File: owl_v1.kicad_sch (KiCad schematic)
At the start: 24 parts, among them J1 USB_C_Receptacle_USB2.0_14P, SW1 SW_SPDT, U1 STM32F103C8T6, U2 XC6206P302, Y1 8MHz, Y2 32k768

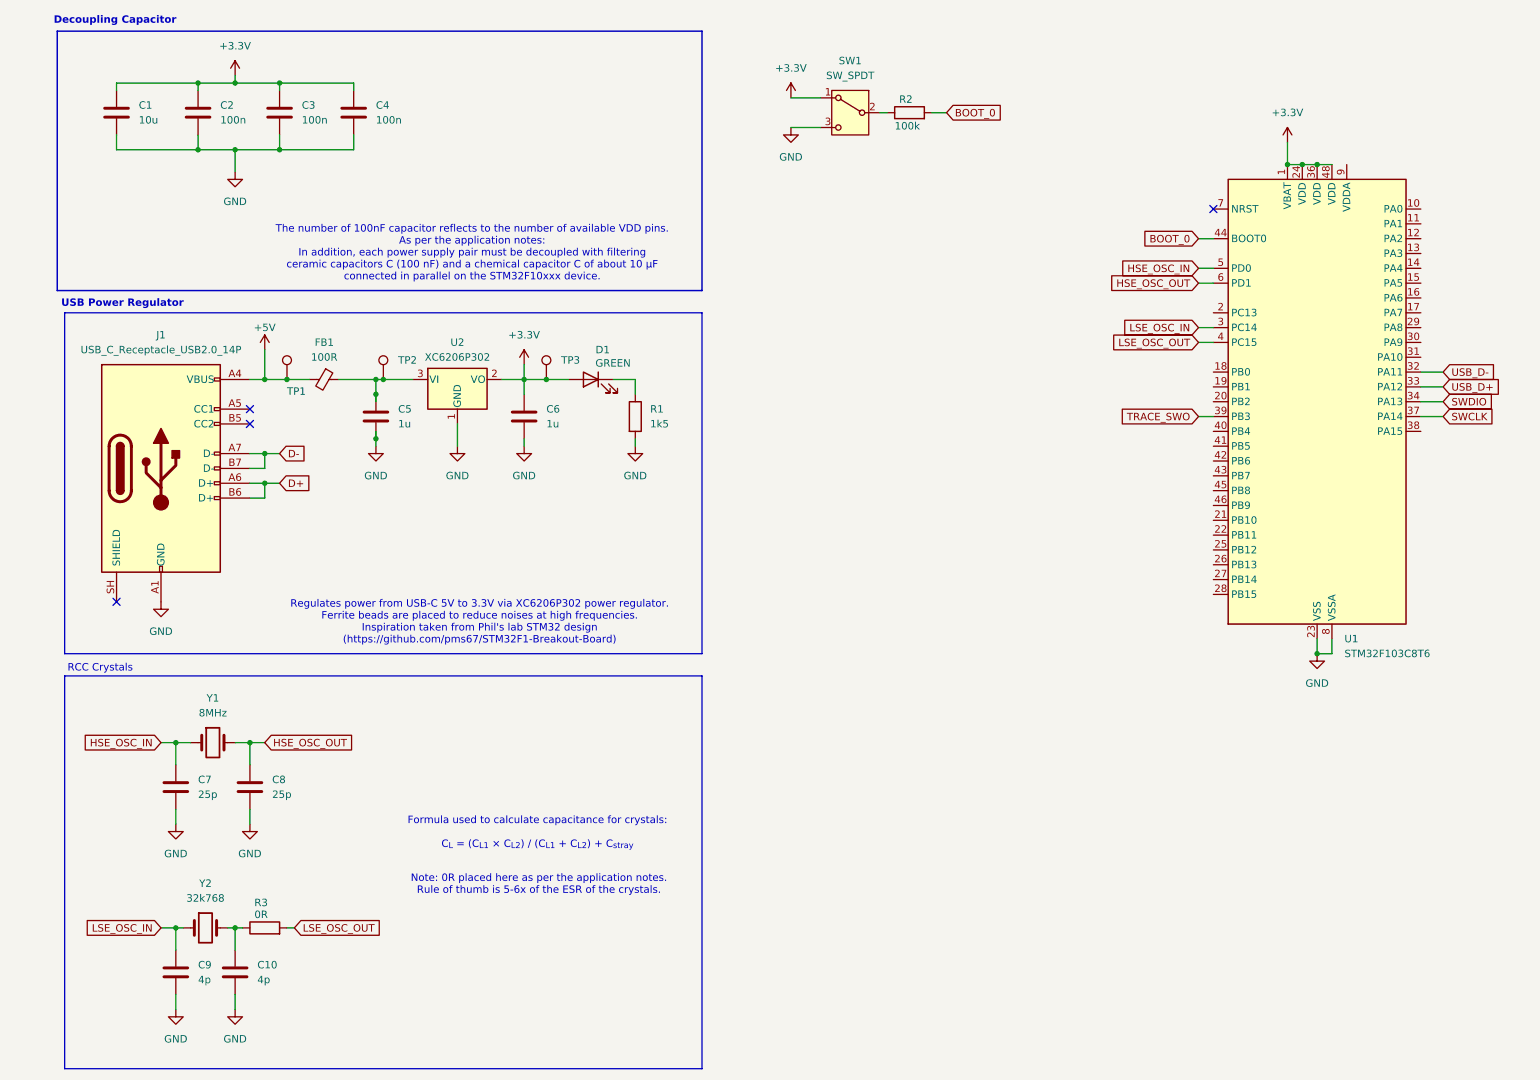
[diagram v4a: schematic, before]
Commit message: [feat] Initial implementation of usb-uart bridge with FT230
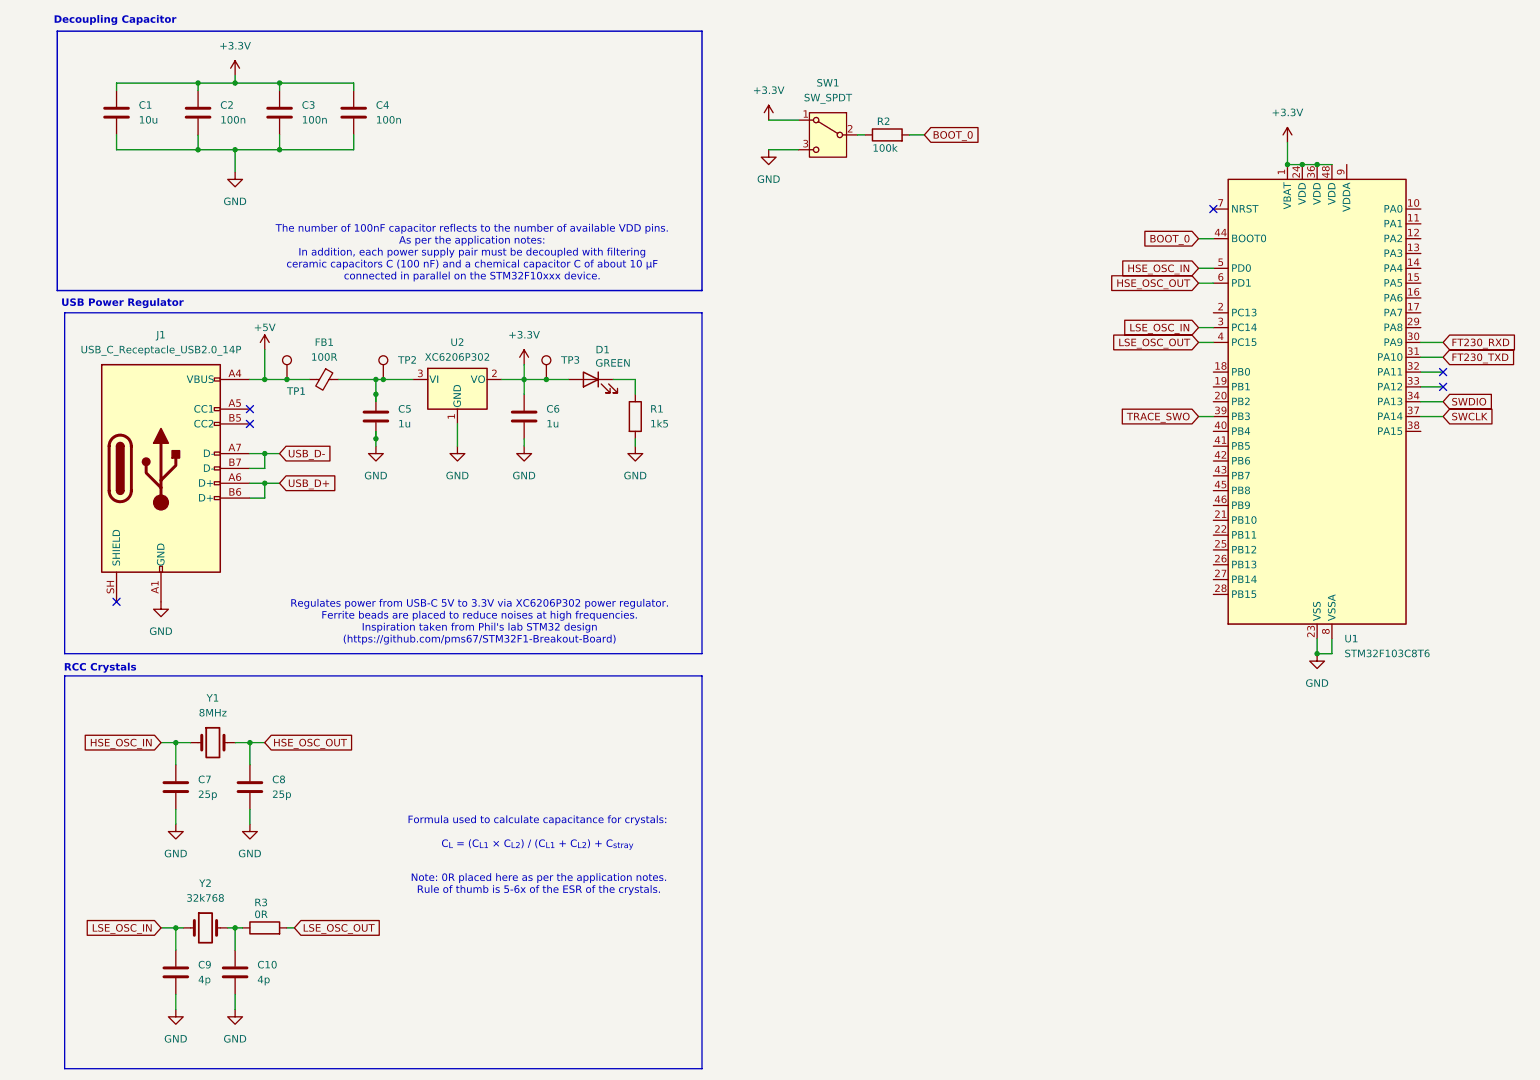
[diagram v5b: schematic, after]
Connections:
- net D+ is gone; now on net USB_D+: J1.A6 (D+), J1.B6 (D+)
- net D- is gone; now on net USB_D-: J1.A7 (D-), J1.B7 (D-)
- net USB_D+: no longer U1.33 (PA12)
- net USB_D-: no longer U1.32 (PA11)
- net FT230_RXD: now reaches U1.30 (PA9)
- net FT230_TXD: now reaches U1.31 (PA10)
- no-connect marks 4 -> 6
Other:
- moved on the sheet: R2, SW1
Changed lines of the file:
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@@
 			(font
 				(size 1.27 1.27)
+				(thickness 0.254)
+				(bold yes)
 			)
 		)
@@
 	)
 	(no_connect
+		(at 260.35 76.2)
+	)
+	(no_connect
 		(at 33.02 115.57)
 	)
@@
 	)
 	(no_connect
+		(at 260.35 78.74)
+	)
+	(no_connect
 		(at 220.98 48.26)
 	)
@@
 	(wire
 		(pts
+			(xy 256.54 73.66) (xy 260.35 73.66)
+		)
+		(stroke
+			(width 0)
+			(type default)
+		)
+	)
+	(wire
+		(pts
 			(xy 77.47 77.47) (xy 78.74 77.47)
 		)
@@
 	(wire
 		(pts
-			(xy 172.72 31.75) (xy 175.26 31.75)
+			(xy 168.91 35.56) (xy 171.45 35.56)
 		)
 		(stroke
@@
 	(wire
 		(pts
-			(xy 148.59 34.29) (xy 153.67 34.29)
+			(xy 144.78 38.1) (xy 149.86 38.1)
 		)
 		(stroke
@@
 	(wire
 		(pts
-			(xy 148.59 29.21) (xy 153.67 29.21)
+			(xy 144.78 33.02) (xy 149.86 33.02)
 		)
 		(stroke
@@
 	(wire
 		(pts
+			(xy 256.54 71.12) (xy 260.35 71.12)
+		)
+		(stroke
+			(width 0)
+			(type default)
+		)
+	)
+	(wire
+		(pts
 			(xy 233.68 36.83) (xy 233.68 40.64)
 		)
@@
 	(wire
 		(pts
-			(xy 163.83 31.75) (xy 165.1 31.75)
+			(xy 160.02 35.56) (xy 161.29 35.56)
 		)
 		(stroke
@@
 		)
 	)
+	(global_label "FT230_TXD"
+		(shape input)
+		(at 260.35 73.66 0)
+		(fields_autoplaced yes)
+		(effects
+			(font
+				(size 1.27 1.27)
+			)
+			(justify left)
+		)
+		(property "Intersheetrefs" "${INTERSHEET_REFS}"
+			(at 273.4346 73.66 0)
+			(hide yes)
+			(show_name no)
+			(do_not_autoplace no)
+			(effects
+				(font
+					(size 1.27 1.27)
+				)
+				(justify left)
+			)
+		)
+	)
 	(global_label "HSE_OSC_OUT"
 		(shape input)
@@
 		)
 	)
-	(global_label "USB_D+"
+	(global_label "FT230_RXD"
 		(shape input)
-		(at 260.35 78.74 0)
+		(at 260.35 71.12 0)
 		(fields_autoplaced yes)
 		(effects
@@
 		)
 		(property "Intersheetrefs" "${INTERSHEET_REFS}"
-			(at 270.9552 78.74 0)
+			(at 273.737 71.12 0)
 			(hide yes)
 			(show_name no)
@@
 		)
 	)
-	(global_label "D+"
+	(global_label "USB_D+"
 		(shape input)
 		(at 60.96 95.25 0)
@@
 		)
 		(property "Intersheetrefs" "${INTERSHEET_REFS}"
-			(at 66.7876 95.25 0)
+			(at 71.5652 95.25 0)
 			(hide yes)
 			(show_name no)
@@
 	(global_label "BOOT_0"
 		(shape input)
-		(at 175.26 31.75 0)
+		(at 171.45 35.56 0)
 		(fields_autoplaced yes)
 		(effects
@@
 		)
 		(property "Intersheetrefs" "${INTERSHEET_REFS}"
-			(at 185.3209 31.75 0)
+			(at 181.5109 35.56 0)
 			(hide yes)
 			(show_name no)
@@
 		)
 	)
-	(global_label "D-"
-		(shape input)
-		(at 60.96 90.17 0)
-		(fields_autoplaced yes)
-		(effects
-			(font
-				(size 1.27 1.27)
-			)
-			(justify left)
-		)
-		(property "Intersheetrefs" "${INTERSHEET_REFS}"
-			(at 66.7876 90.17 0)
-			(hide yes)
-			(show_name no)
-			(do_not_autoplace no)
-			(effects
-				(font
-					(size 1.27 1.27)
-				)
-				(justify left)
-			)
-		)
-	)
 	(global_label "USB_D-"
 		(shape input)
-		(at 260.35 76.2 0)
+		(at 60.96 90.17 0)
 		(fields_autoplaced yes)
 		(effects
@@
 		)
 		(property "Intersheetrefs" "${INTERSHEET_REFS}"
-			(at 270.9552 76.2 0)
+			(at 71.5652 90.17 0)
 			(hide yes)
 			(show_name no)
@@
 	(symbol
 		(lib_id "power:+3.3V")
-		(at 148.59 29.21 0)
+		(at 144.78 33.02 0)
 		(unit 1)
 		(body_style 1)
@@
 		(fields_autoplaced yes)
 		(property "Reference" "#PWR012"
-			(at 148.59 33.02 0)
+			(at 144.78 36.83 0)
 			(hide yes)
 			(show_name no)
@@
 		)
 		(property "Value" "+3.3V"
-			(at 148.59 24.13 0)
+			(at 144.78 27.94 0)
 			(show_name no)
 			(do_not_autoplace no)
@@
 		)
 		(property "Footprint" ""
-			(at 148.59 29.21 0)
+			(at 144.78 33.02 0)
 			(hide yes)
 			(show_name no)
@@
 		)
 		(property "Datasheet" ""
-			(at 148.59 29.21 0)
+			(at 144.78 33.02 0)
 			(hide yes)
 			(show_name no)
@@
 		)
 		(property "Description" "Power symbol creates a global label with name \"+3.3V\""
-			(at 148.59 29.21 0)
+			(at 144.78 33.02 0)
 			(hide yes)
 			(show_name no)
@@
 	(symbol
 		(lib_id "power:GND")
-		(at 148.59 34.29 0)
+		(at 144.78 38.1 0)
 		(unit 1)
 		(body_style 1)
@@
 		(fields_autoplaced yes)
 		(property "Reference" "#PWR013"
-			(at 148.59 40.64 0)
+			(at 144.78 44.45 0)
 			(hide yes)
 			(show_name no)
@@
 		)
 		(property "Value" "GND"
-			(at 148.59 39.37 0)
+			(at 144.78 43.18 0)
 			(show_name no)
 			(do_not_autoplace no)
@@
 		)
 		(property "Footprint" ""
-			(at 148.59 34.29 0)
+			(at 144.78 38.1 0)
 			(hide yes)
 			(show_name no)
@@
 		)
 		(property "Datasheet" ""
-			(at 148.59 34.29 0)
+			(at 144.78 38.1 0)
 			(hide yes)
 			(show_name no)
@@
 		)
 		(property "Description" "Power symbol creates a global label with name \"GND\" , ground"
-			(at 148.59 34.29 0)
+			(at 144.78 38.1 0)
 			(hide yes)
 			(show_name no)
@@
 	(symbol
 		(lib_id "Switch:SW_SPDT")
-		(at 158.75 31.75 0)
+		(at 154.94 35.56 0)
 		(mirror y)
 		(unit 1)
@@
 		(dnp no)
 		(property "Reference" "SW1"
-			(at 158.75 22.86 0)
+			(at 154.94 26.67 0)
 			(show_name no)
 			(do_not_autoplace no)
@@
 		)
 		(property "Value" "SW_SPDT"
-			(at 158.75 25.4 0)
+			(at 154.94 29.21 0)
 			(show_name no)
 			(do_not_autoplace no)
@@
 		)
 		(property "Footprint" ""
-			(at 158.75 31.75 0)
+			(at 154.94 35.56 0)
 			(hide yes)
 			(show_name no)
@@
 		)
 		(property "Datasheet" ""
-			(at 158.75 39.37 0)
+			(at 154.94 43.18 0)
 			(hide yes)
 			(show_name no)
@@
 		)
 		(property "Description" "Switch, single pole double throw"
-			(at 158.75 31.75 0)
+			(at 154.94 35.56 0)
 			(hide yes)
 			(show_name no)
@@
 	(symbol
 		(lib_id "Device:R")
-		(at 168.91 31.75 90)
+		(at 165.1 35.56 90)
 		(unit 1)
 		(body_style 1)
@@
 		(dnp no)
 		(property "Reference" "R2"
-			(at 167.132 29.464 90)
+			(at 163.322 33.274 90)
 			(show_name no)
 			(do_not_autoplace no)
@@
 		)
 		(property "Value" "100k"
-			(at 166.37 34.036 90)
+			(at 162.56 37.846 90)
 			(show_name no)
 			(do_not_autoplace no)
@@
 		)
 		(property "Footprint" ""
-			(at 168.91 33.528 90)
+			(at 165.1 37.338 90)
 			(hide yes)
 			(show_name no)
@@
 		)
 		(property "Datasheet" ""
-			(at 168.91 31.75 0)
+			(at 165.1 35.56 0)
 			(hide yes)
 			(show_name no)
@@
 		)
 		(property "Description" "Resistor"
-			(at 168.91 31.75 0)
+			(at 165.1 35.56 0)
 			(hide yes)
 			(show_name no)

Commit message: [refactor] Refactor the schematics to use sub-sheets
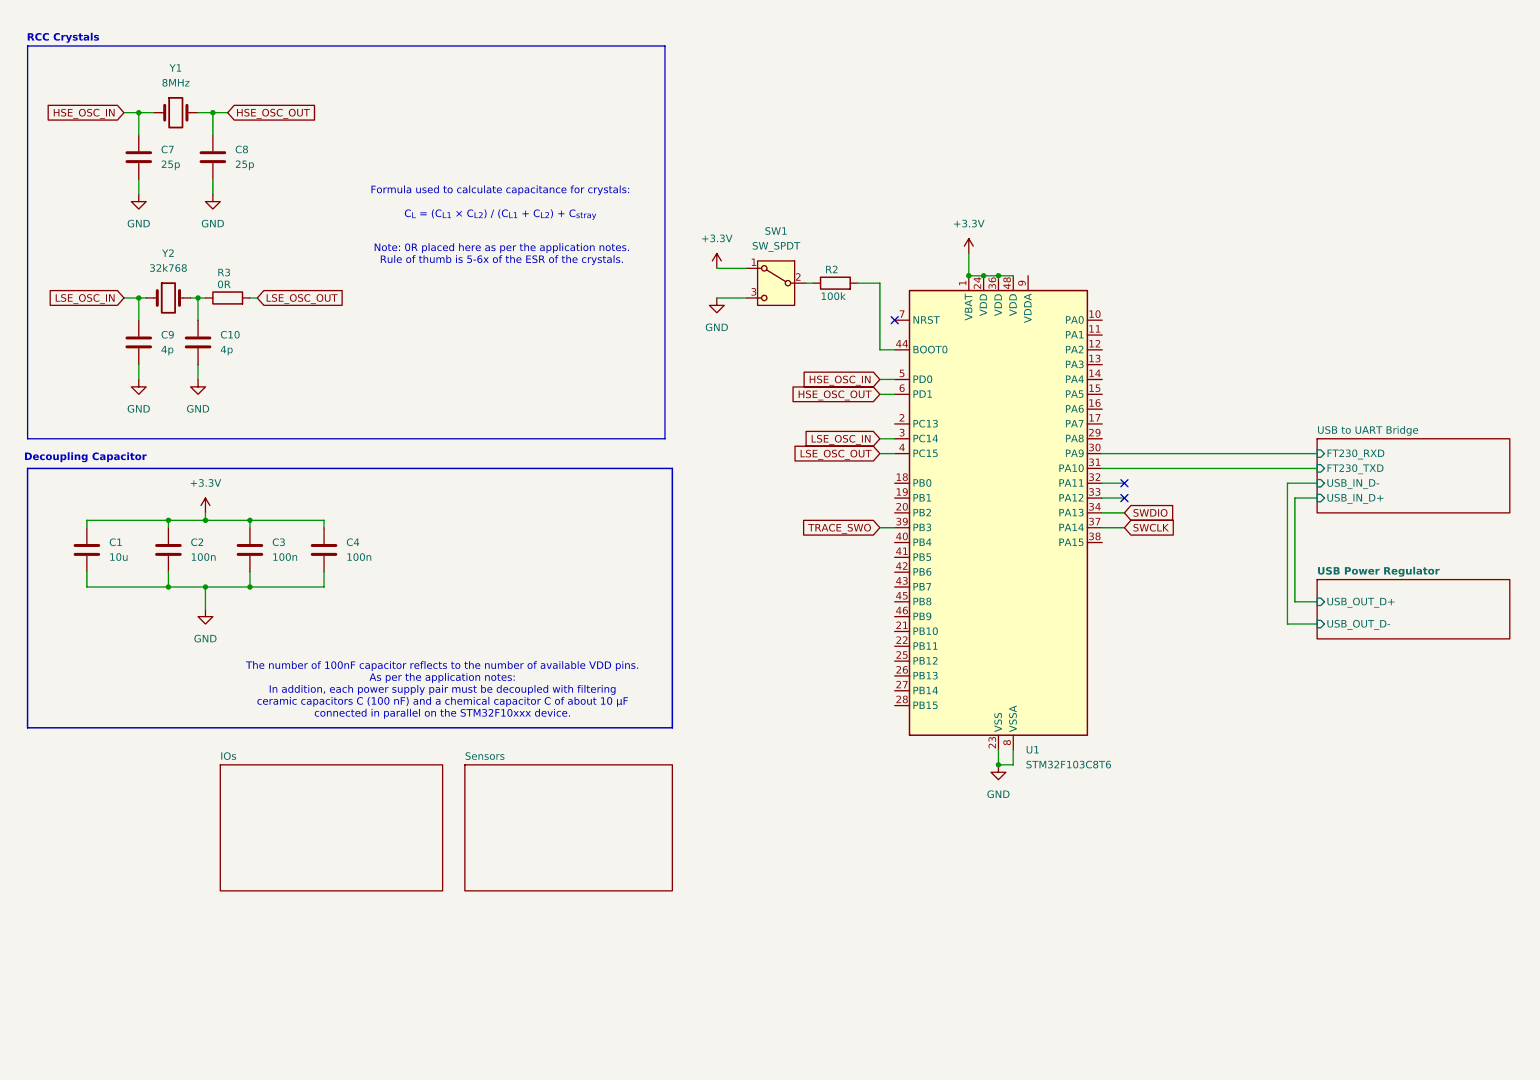
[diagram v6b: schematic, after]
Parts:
- removed C5, C6: 1u, Capacitor_SMD:C_0603_1608Metric, symbol Device:C
- removed D1: GREEN, LED_SMD:LED_0603_1608Metric, symbol Device:LED
- removed FB1: 100R, Inductor_SMD:L_0603_1608Metric, symbol Device:FerriteBead_Small
- removed J1: USB_C_Receptacle_USB2.0_14P, symbol Connector:USB_C_Receptacle_USB2.0_14P
- removed R1: 1k5, Resistor_SMD:R_0603_1608Metric, symbol Device:R
- removed TP1, TP2, TP3: (no value), symbol Connector:TestPoint
- removed U2: XC6206P302, Package_TO_SOT_SMD:SOT-23-3, symbol Regulator_Linear:XC6206PxxxMR
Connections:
- net BOOT_0: no longer names the net of R2.2, U1.44 (BOOT0)
- net FT230_RXD renamed USB to UART Bridge/FT230_RXD
- net FT230_TXD renamed USB to UART Bridge/FT230_TXD
- no-connect marks 6 -> 3
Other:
- added sheet IOs (GPIOs.kicad_sch)
- added sheet Sensors (sensors.kicad_sch)
- added sheet USB Power Regulator (usb_power_regulator.kicad_sch)
- added sheet USB to UART Bridge (usb_to_uart.kicad_sch)
- note removed: "Regulates power from USB-C 5V to 3.3V via XC6206P302 power regulator. Ferrite beads are placed to reduce noises at high frequencies. Inspiration taken from Phil's lab STM32 design (https://github.com/pms67/STM32F1-Breakout-Board)"
- note removed: "USB Power Regulator"
- moved on the sheet: C10, C7, C8, C9, R2, R3, SW1, U1, Y1, Y2

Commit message: [feat] Add CAN transceiver SN65VHD230
Also ran ERC checks and add some exclusion ERC for the FT230XS due to
3V3OUT being an input pin rather than output pin
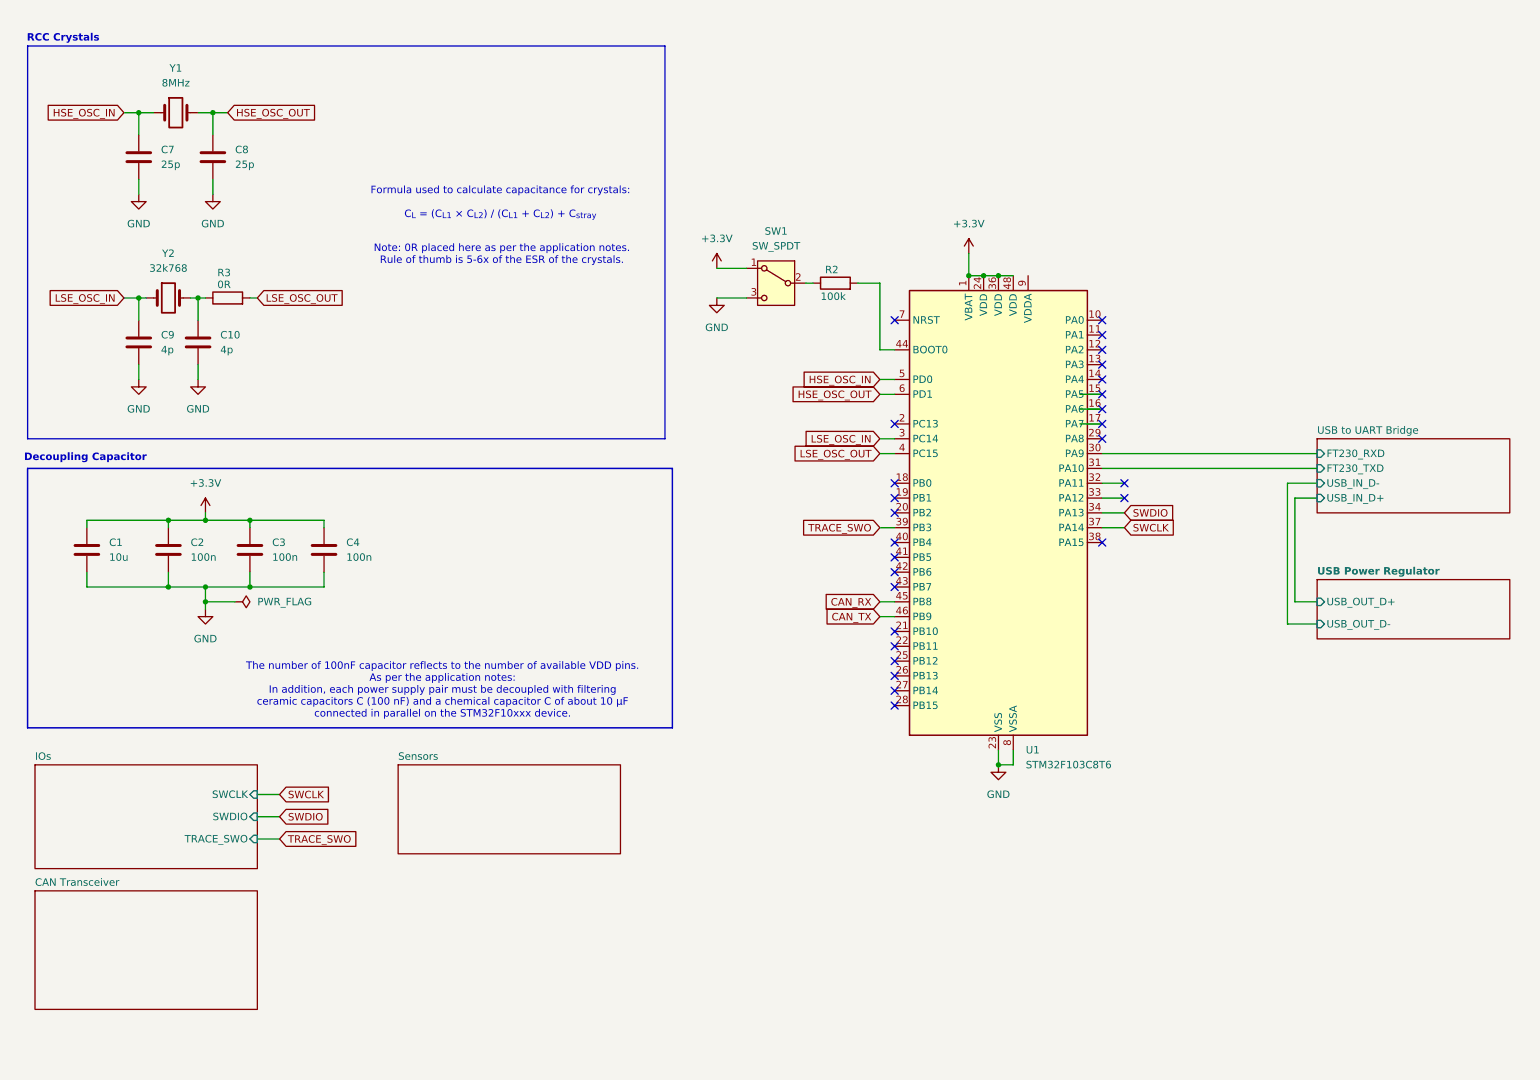
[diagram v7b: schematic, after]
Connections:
- net CAN_RX: now reaches U1.45 (PB8)
- net CAN_TX: now reaches U1.46 (PB9)
- no-connect marks 3 -> 27
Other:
- added sheet CAN Transceiver (can_controller.kicad_sch)
- sheet IOs ports: added SWCLK, SWDIO, TRACE_SWO; removed none
